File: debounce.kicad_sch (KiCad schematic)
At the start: 7 parts, among them U4 74HC14

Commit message: Adjust some footprints and PCB settings
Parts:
- D7: footprint LED_THT:LED_D3.0mm_Horizontal_O6.35mm_Z2.0mm -> LED_THT:LED_D3.0mm_Horizontal_O3.81mm_Z2.0mm
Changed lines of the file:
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@@
 	(title_block
 		(title "Smart Home Energy Metering")
-		(date "2025-06-10")
+		(date "2025-06-15")
 		(rev "1.0")
 		(comment 1 "https://github.com/zargony/smarthome-metering")
@@
 			)
 		)
-		(property "Footprint" "LED_THT:LED_D3.0mm_Horizontal_O6.35mm_Z2.0mm"
+		(property "Footprint" "LED_THT:LED_D3.0mm_Horizontal_O3.81mm_Z2.0mm"
 			(at 101.6 78.74 0)
 			(effects

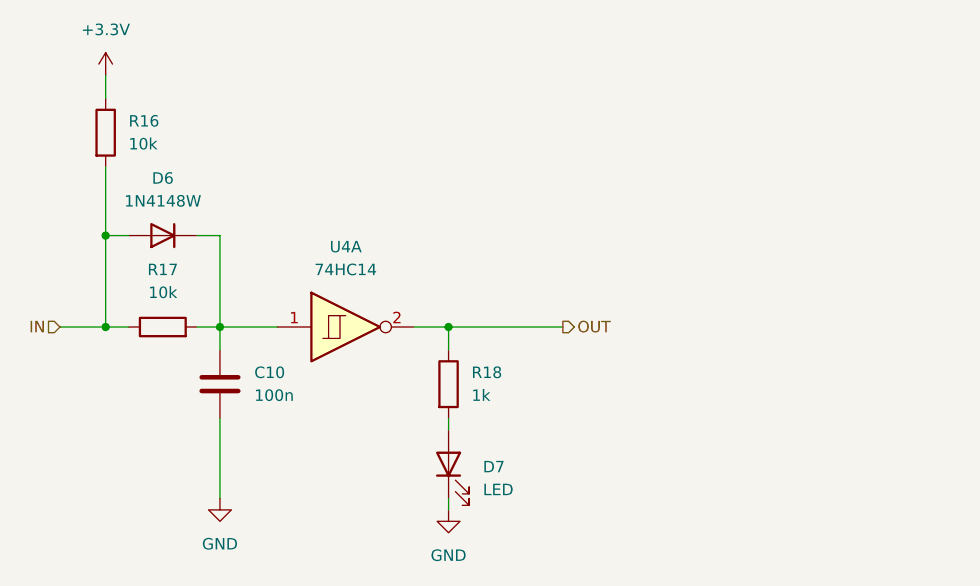
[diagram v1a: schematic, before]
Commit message: Remove UART Tx LED
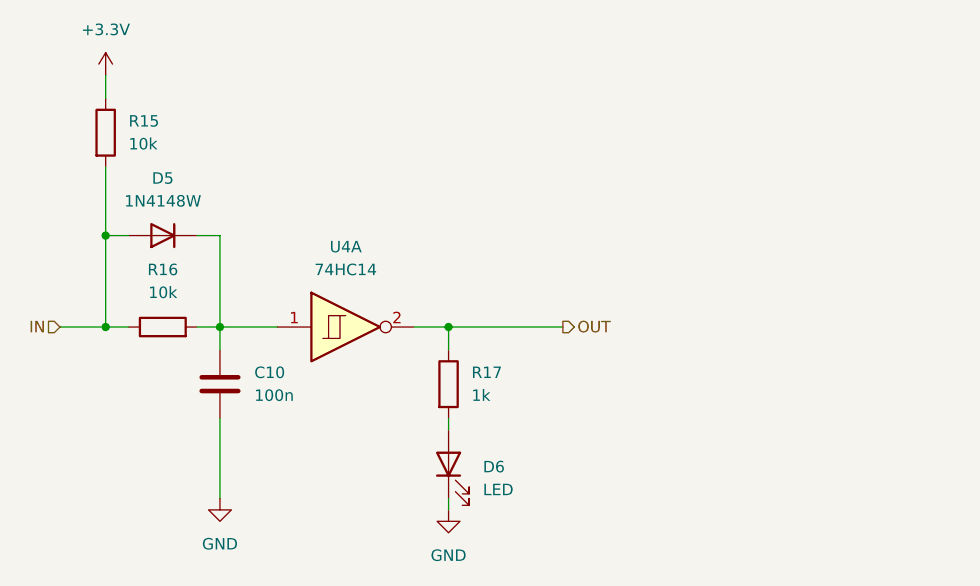
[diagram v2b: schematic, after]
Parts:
- D6: renamed from D7; footprint LED_THT:LED_D3.0mm_Horizontal_O3.81mm_Z2.0mm -> LED_THT:LED_D3.0mm
- renumbered D6 to D5, R16 to R15, R17 to R16, R18 to R17
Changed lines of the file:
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@@
 	(title_block
 		(title "Smart Home Energy Metering")
-		(date "2025-06-15")
+		(date "2025-06-16")
 		(rev "1.0")
 		(comment 1 "https://github.com/zargony/smarthome-metering")
@@
 		(dnp no)
 		(fields_autoplaced yes)
-		(property "Reference" "R18"
+		(property "Reference" "R17"
 			(at 104.14 68.5799 0)
 			(effects
@@
 			(project "metering"
 				(path "/2132c704-8b90-4a68-a04d-0b4be367d67b/aff1b94e-69ca-420a-a7c4-8c8197c0a1fd"
-					(reference "R18")
+					(reference "R17")
 					(unit 1)
 				)
 				(path "/2132c704-8b90-4a68-a04d-0b4be367d67b/e1a8ed28-192d-42ff-b7d9-d46b9b3862c7"
-					(reference "R21")
+					(reference "R20")
 					(unit 1)
 				)
 				(path "/2132c704-8b90-4a68-a04d-0b4be367d67b/fc1b8e3c-9114-4782-b79d-e6339273f4a3"
-					(reference "R24")
+					(reference "R23")
 					(unit 1)
 				)
@@
 		(dnp no)
 		(fields_autoplaced yes)
-		(property "Reference" "R17"
+		(property "Reference" "R16"
 			(at 69.85 57.15 90)
 			(effects
@@
 			(project "metering"
 				(path "/2132c704-8b90-4a68-a04d-0b4be367d67b/aff1b94e-69ca-420a-a7c4-8c8197c0a1fd"
-					(reference "R17")
+					(reference "R16")
 					(unit 1)
 				)
 				(path "/2132c704-8b90-4a68-a04d-0b4be367d67b/e1a8ed28-192d-42ff-b7d9-d46b9b3862c7"
-					(reference "R20")
+					(reference "R19")
 					(unit 1)
 				)
 				(path "/2132c704-8b90-4a68-a04d-0b4be367d67b/fc1b8e3c-9114-4782-b79d-e6339273f4a3"
-					(reference "R23")
+					(reference "R22")
 					(unit 1)
 				)
@@
 		(dnp no)
 		(fields_autoplaced yes)
-		(property "Reference" "R16"
+		(property "Reference" "R15"
 			(at 66.04 40.64 0)
 			(effects
@@
 			(project "metering"
 				(path "/2132c704-8b90-4a68-a04d-0b4be367d67b/aff1b94e-69ca-420a-a7c4-8c8197c0a1fd"
-					(reference "R16")
+					(reference "R15")
 					(unit 1)
 				)
 				(path "/2132c704-8b90-4a68-a04d-0b4be367d67b/e1a8ed28-192d-42ff-b7d9-d46b9b3862c7"
-					(reference "R19")
+					(reference "R18")
 					(unit 1)
 				)
 				(path "/2132c704-8b90-4a68-a04d-0b4be367d67b/fc1b8e3c-9114-4782-b79d-e6339273f4a3"
-					(reference "R22")
+					(reference "R21")
 					(unit 1)
 				)
@@
 		(dnp no)
 		(fields_autoplaced yes)
-		(property "Reference" "D7"
+		(property "Reference" "D6"
 			(at 105.41 79.0574 90)
 			(effects
@@
 			)
 		)
-		(property "Footprint" "LED_THT:LED_D3.0mm_Horizontal_O3.81mm_Z2.0mm"
+		(property "Footprint" "LED_THT:LED_D3.0mm"
 			(at 101.6 78.74 0)
 			(effects
@@
 			(project "metering"
 				(path "/2132c704-8b90-4a68-a04d-0b4be367d67b/aff1b94e-69ca-420a-a7c4-8c8197c0a1fd"
-					(reference "D7")
+					(reference "D6")
 					(unit 1)
 				)
 				(path "/2132c704-8b90-4a68-a04d-0b4be367d67b/e1a8ed28-192d-42ff-b7d9-d46b9b3862c7"
-					(reference "D9")
+					(reference "D8")
 					(unit 1)
 				)
 				(path "/2132c704-8b90-4a68-a04d-0b4be367d67b/fc1b8e3c-9114-4782-b79d-e6339273f4a3"
-					(reference "D11")
+					(reference "D10")
 					(unit 1)
 				)
@@
 		(dnp no)
 		(fields_autoplaced yes)
-		(property "Reference" "D6"
+		(property "Reference" "D5"
 			(at 69.85 46.99 0)
 			(effects
@@
 			(project "metering"
 				(path "/2132c704-8b90-4a68-a04d-0b4be367d67b/aff1b94e-69ca-420a-a7c4-8c8197c0a1fd"
-					(reference "D6")
+					(reference "D5")
 					(unit 1)
 				)
 				(path "/2132c704-8b90-4a68-a04d-0b4be367d67b/e1a8ed28-192d-42ff-b7d9-d46b9b3862c7"
-					(reference "D8")
+					(reference "D7")
 					(unit 1)
 				)
 				(path "/2132c704-8b90-4a68-a04d-0b4be367d67b/fc1b8e3c-9114-4782-b79d-e6339273f4a3"
-					(reference "D10")
-					(unit 1)
-				)
+					(reference "D9")
+					(unit 1)
+				)

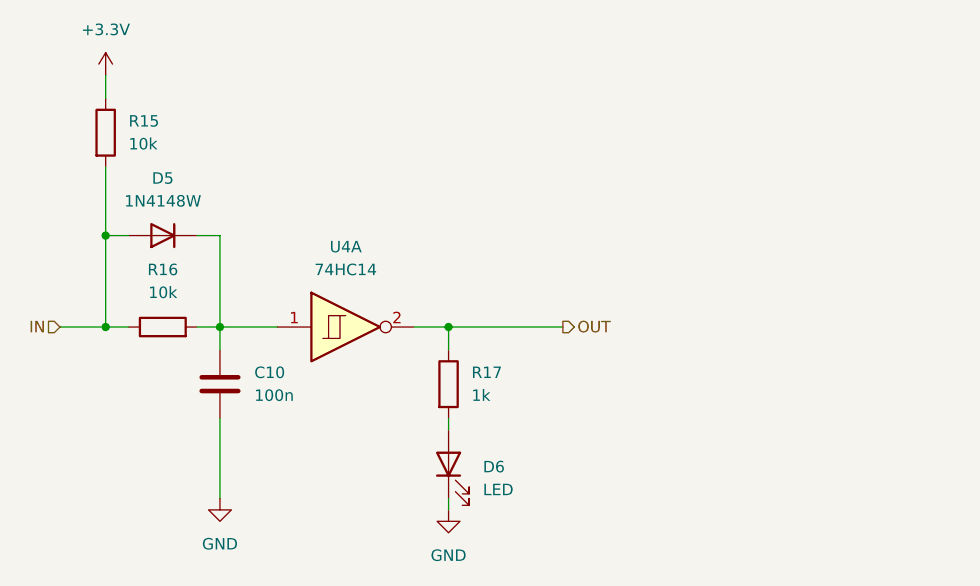
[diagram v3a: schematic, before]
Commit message: Add comment about debounce time calculation
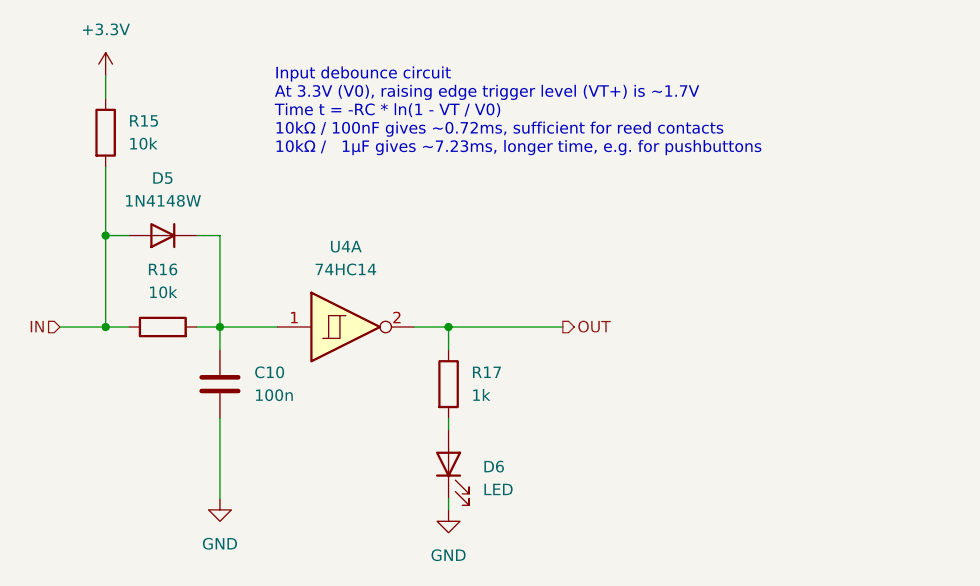
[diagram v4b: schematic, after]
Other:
- note added: "Input debounce circuit At 3.3V (V0), raising edge trigger level (VT+) is ~1.7V Time t = -RC * ln(1 - VT / V0) 10kΩ / 100nF gives ~0.72ms, sufficient for reed contacts 10kΩ / 1µF gives ~7.23ms, longer time, e.g. for pushbuttons"
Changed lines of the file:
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@@
 		(comment 1 "https://github.com/zargony/smarthome-metering")
+	)
+	(text "Input debounce circuit\nAt 3.3V (V0), raising edge trigger level (VT+) is ~1.7V\nTime t = -RC * ln(1 - VT / V0)\n10kΩ / 100nF gives ~0.72ms, sufficient for reed contacts\n10kΩ /   1µF gives ~7.23ms, longer time, e.g. for pushbuttons\n"
+		(exclude_from_sim no)
+		(at 82.296 44.45 0)
+		(effects
+			(font
+				(size 1.27 1.27)
+				(thickness 0.1588)
+			)
+			(justify left bottom)
+		)
 	)
 	(junction

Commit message: Improve schematic style
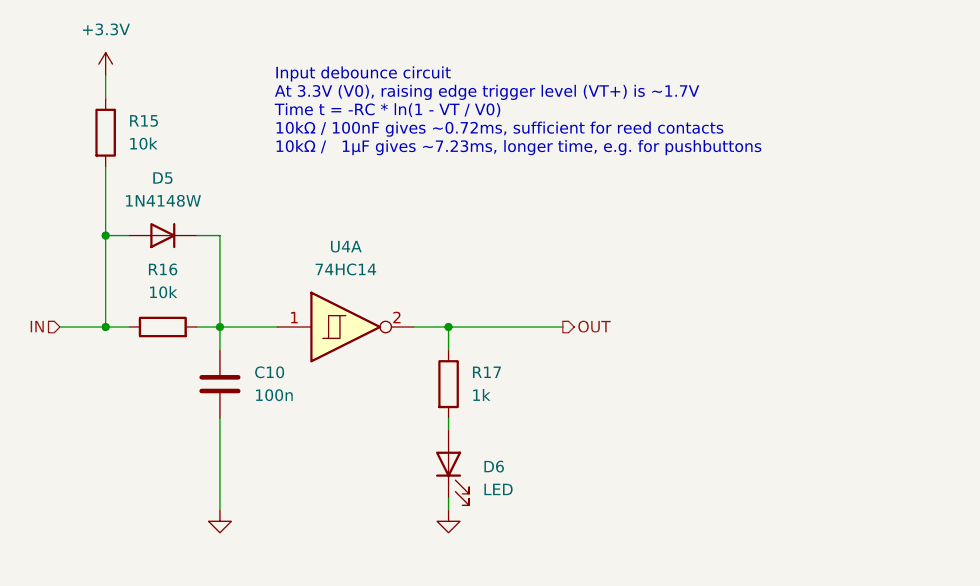
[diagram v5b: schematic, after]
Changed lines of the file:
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@@
 	(wire
 		(pts
-			(xy 76.2 73.66) (xy 76.2 82.55)
+			(xy 76.2 73.66) (xy 76.2 83.82)
 		)
 		(stroke
@@
 	(symbol
 		(lib_id "power:GND")
-		(at 76.2 82.55 0)
+		(at 76.2 83.82 0)
 		(unit 1)
 		(exclude_from_sim no)
@@
 		(fields_autoplaced yes)
 		(property "Reference" "#PWR041"
+			(at 76.2 90.17 0)
+			(effects
+				(font
+					(size 1.27 1.27)
+				)
+				(hide yes)
+			)
+		)
+		(property "Value" "GND"
 			(at 76.2 88.9 0)
 			(effects
@@
 			)
 		)
-		(property "Value" "GND"
-			(at 76.2 87.63 0)
-			(effects
-				(font
-					(size 1.27 1.27)
-				)
-			)
-		)
 		(property "Footprint" ""
-			(at 76.2 82.55 0)
+			(at 76.2 83.82 0)
 			(effects
 				(font
@@
 		)
 		(property "Datasheet" ""
-			(at 76.2 82.55 0)
+			(at 76.2 83.82 0)
 			(effects
 				(font
@@
 		)
 		(property "Description" "Power symbol creates a global label with name \"GND\" , ground"
-			(at 76.2 82.55 0)
+			(at 76.2 83.82 0)
 			(effects
 				(font
@@
 					(size 1.27 1.27)
 				)
-			)
-		)
+				(hide yes)
+			)
+		)

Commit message: Update debounce time calculation
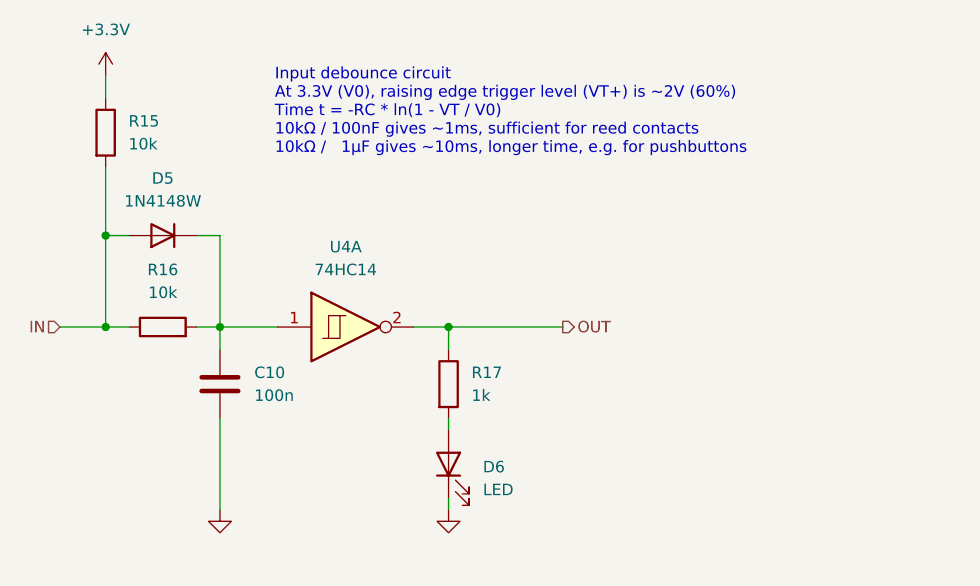
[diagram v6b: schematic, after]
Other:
- note added: "Input debounce circuit At 3.3V (V0), raising edge trigger level (VT+) is ~2V (60%) Time t = -RC * ln(1 - VT / V0) 10kΩ / 100nF gives ~1ms, sufficient for reed contacts 10kΩ / 1µF gives ~10ms, longer time, e.g. for pushbuttons"
- note removed: "Input debounce circuit At 3.3V (V0), raising edge trigger level (VT+) is ~1.7V Time t = -RC * ln(1 - VT / V0) 10kΩ / 100nF gives ~0.72ms, sufficient for reed contacts 10kΩ / 1µF gives ~7.23ms, longer time, e.g. for pushbuttons"
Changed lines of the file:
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@@
 	(title_block
 		(title "Smart Home Energy Metering")
-		(date "2025-06-18")
+		(date "2025-06-27")
 		(rev "1.0")
 		(comment 1 "https://github.com/zargony/smarthome-metering")
 	)
-	(text "Input debounce circuit\nAt 3.3V (V0), raising edge trigger level (VT+) is ~1.7V\nTime t = -RC * ln(1 - VT / V0)\n10kΩ / 100nF gives ~0.72ms, sufficient for reed contacts\n10kΩ /   1µF gives ~7.23ms, longer time, e.g. for pushbuttons\n"
+	(text "Input debounce circuit\nAt 3.3V (V0), raising edge trigger level (VT+) is ~2V (60%)\nTime t = -RC * ln(1 - VT / V0)\n10kΩ / 100nF gives ~1ms, sufficient for reed contacts\n10kΩ /   1µF gives ~10ms, longer time, e.g. for pushbuttons\n"
 		(exclude_from_sim no)
 		(at 82.296 44.45 0)
